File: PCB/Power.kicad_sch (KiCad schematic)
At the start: 27 parts, among them U2 XL4005E1, U3 NCP1117-3.3_SOT223

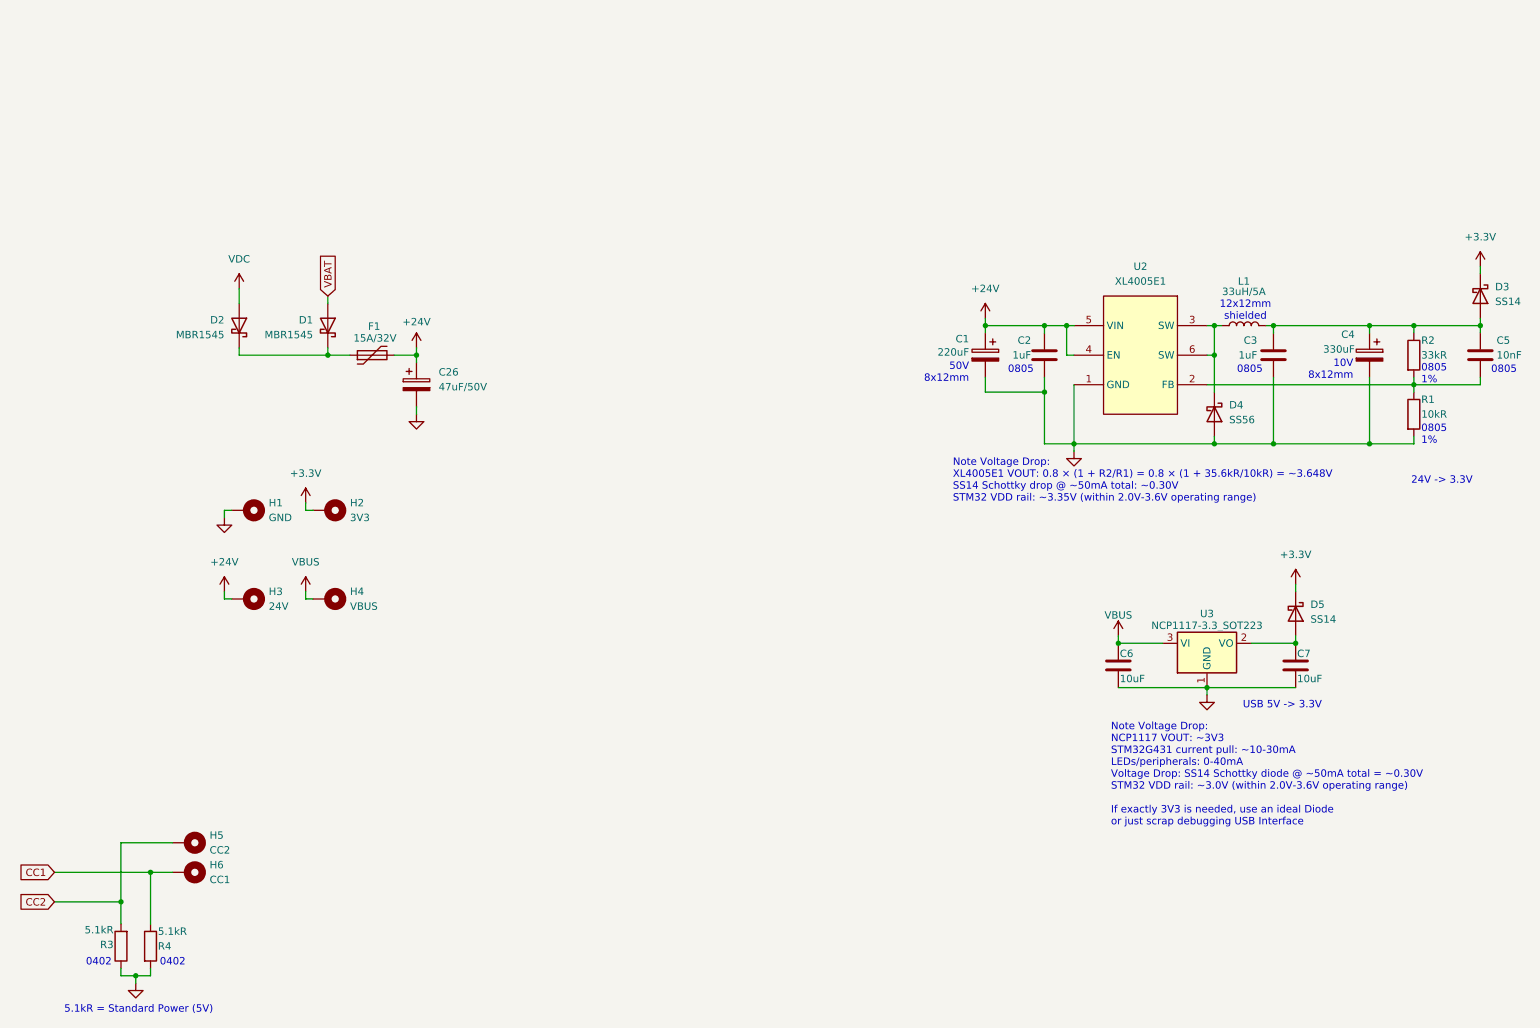
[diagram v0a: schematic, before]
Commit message: Improved Protection and Board Testability - Added power rail protection and decoupling for stepper motor noise environment - Added TVS, bulk caps and fuse upgrade on 24V rail - Added test pads for bring-up and debugging
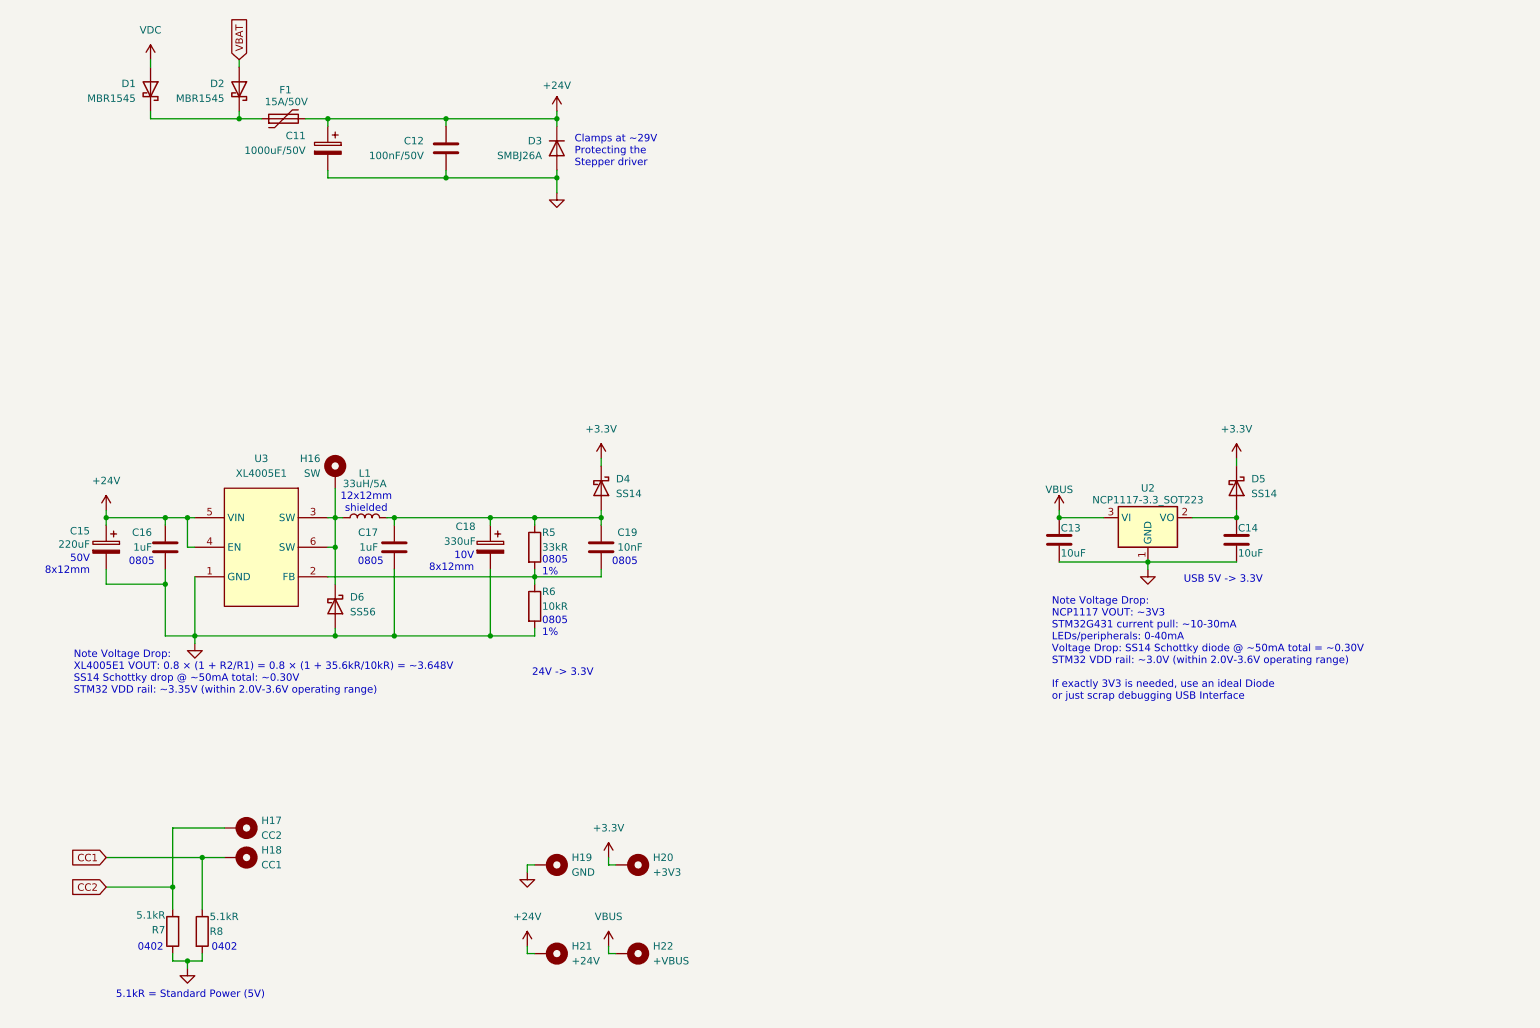
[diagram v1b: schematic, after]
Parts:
- added C12: 100nF/50V, Capacitor_SMD:C_0402_1005Metric, symbol Device:C
- added D3: SMBJ26A, Diode_SMD:D_SMB, symbol Device:D
- added H16: SW, TestPoint:TestPoint_Pad_D1.0mm, symbol Mechanical:MountingHole_Pad
- C11: renamed from C26; value 47uF/50V -> 1000uF/50V; footprint Capacitor_THT:CP_Radial_D8.0mm_P3.50mm -> Capacitor_THT:CP_Radial_D10.0mm_P5.00mm
- F1: value 15A/32V -> 15A/50V
- H17: renamed from H5; footprint TestPoint:TestPoint_Pad_D1.5mm -> TestPoint:TestPoint_Pad_D2.0mm
- H18: renamed from H6; footprint TestPoint:TestPoint_Pad_D1.5mm -> TestPoint:TestPoint_Pad_D2.0mm
- H19: renamed from H1; footprint TestPoint:TestPoint_Pad_D1.5mm -> TestPoint:TestPoint_Pad_D2.0mm
- H20: renamed from H2; value 3V3 -> +3V3; footprint TestPoint:TestPoint_Pad_D1.5mm -> TestPoint:TestPoint_Pad_D2.0mm
- H21: renamed from H3; value 24V -> +24V; footprint TestPoint:TestPoint_Pad_D1.5mm -> TestPoint:TestPoint_Pad_D2.0mm
- H22: renamed from H4; value VBUS -> +VBUS; footprint TestPoint:TestPoint_Pad_D1.5mm -> TestPoint:TestPoint_Pad_D2.0mm
- renumbered C6 to C13, C7 to C14, C1 to C15, C2 to C16, C3 to C17, C4 to C18, C5 to C19, D2 to D1, D1 to D2, D3 to D4, D4 to D6, R2 to R5, R1 to R6, R3 to R7, R4 to R8, U3 to U2, U2 to U3
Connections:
- net +24V: now also C12.1, D3.1 (K)
- net GND: now also C12.2, D3.2 (A)
- net at D6.1 (K), L1.1, U3.3 (SW)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: now also H16.1
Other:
- note added: "Clamps at ~29V Protecting the Stepper driver"
- moved on the sheet: C11, C13, C14, C15, C16, C17, C18, C19, D1, D2, D4, D5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

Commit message: Started laying out the PCB - Decided for a square-shaped board - Split Motor Controllers on top and bottom - Split Power Plane (+3V3 on logic side, +24V on motor side) - Roughly layed out the board entirely - Reconsidered my life choises (got sick)
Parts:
- removed H21: +24V, TestPoint:TestPoint_Pad_D2.0mm, symbol Mechanical:MountingHole_Pad
- added C70: 100nF/50V, Capacitor_SMD:C_0603_1608Metric, symbol Device:C
- added D10: SMBJ26A, Diode_SMD:D_SMB, symbol Device:D
- added H20, H35, H37, H38: +24V, TestPoint:TestPoint_Pad_D2.0mm, symbol Mechanical:MountingHole_Pad
- added H36, H39, H40: GND, TestPoint:TestPoint_Pad_D2.0mm, symbol Mechanical:MountingHole_Pad
- C15: renamed from C12; footprint Capacitor_SMD:C_0402_1005Metric -> Capacitor_SMD:C_0603_1608Metric
- H16: renamed from H17; footprint TestPoint:TestPoint_Pad_D2.0mm -> TestPoint:TestPoint_Pad_D1.0mm
- H17: renamed from H18; footprint TestPoint:TestPoint_Pad_D2.0mm -> TestPoint:TestPoint_Pad_D1.0mm
- renumbered C15 to C11, C16 to C12, C11 to C13, C17 to C14, C18 to C16, C19 to C17, C13 to C18, C14 to C19, D6 to D3, D3 to D4, D4 to D5, D5 to D6, H16 to H18, H20 to H21, R7 to R5, R8 to R6, R5 to R7, R6 to R8, U3 to U2, U2 to U3
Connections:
- net +24V: now also C70.1, D10.1 (K), H20.1, H35.1, H37.1, H38.1
- net GND: now also C70.2, D10.2 (A), H36.1, H39.1, H40.1
- net BIDIR_24V: now reaches D1.1 (K), D2.1 (K), F1.1
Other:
- moved on the sheet: C13, C15, D1, D2, D4, F1, H19, H21, H22

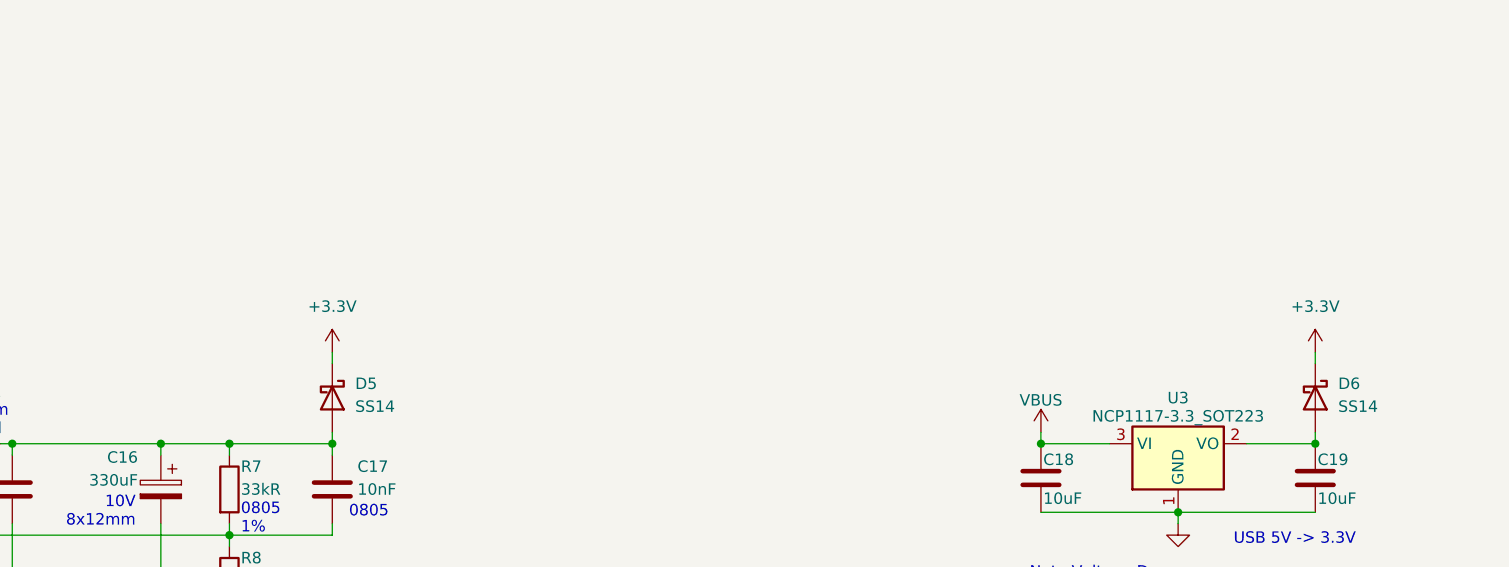
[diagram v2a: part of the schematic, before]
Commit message: Continued PCB Development - Routed MCU decoupeling and Isolated Crystal - Routed LDO Buck converter (VBUS (+5V) -> +3V3) - Routed Buck Converter (+24V -> +3V3) needs review (U2-pin1-GND) - Started Routing TMC2209 to their terminal blocks - Noticed issue with Stepper Lines coupeling back into +24V - TODO: Move Motor Input farther inside and add grounding isolation - Fixed Polariy mismatch with J3 (XT60 Battery Connector)
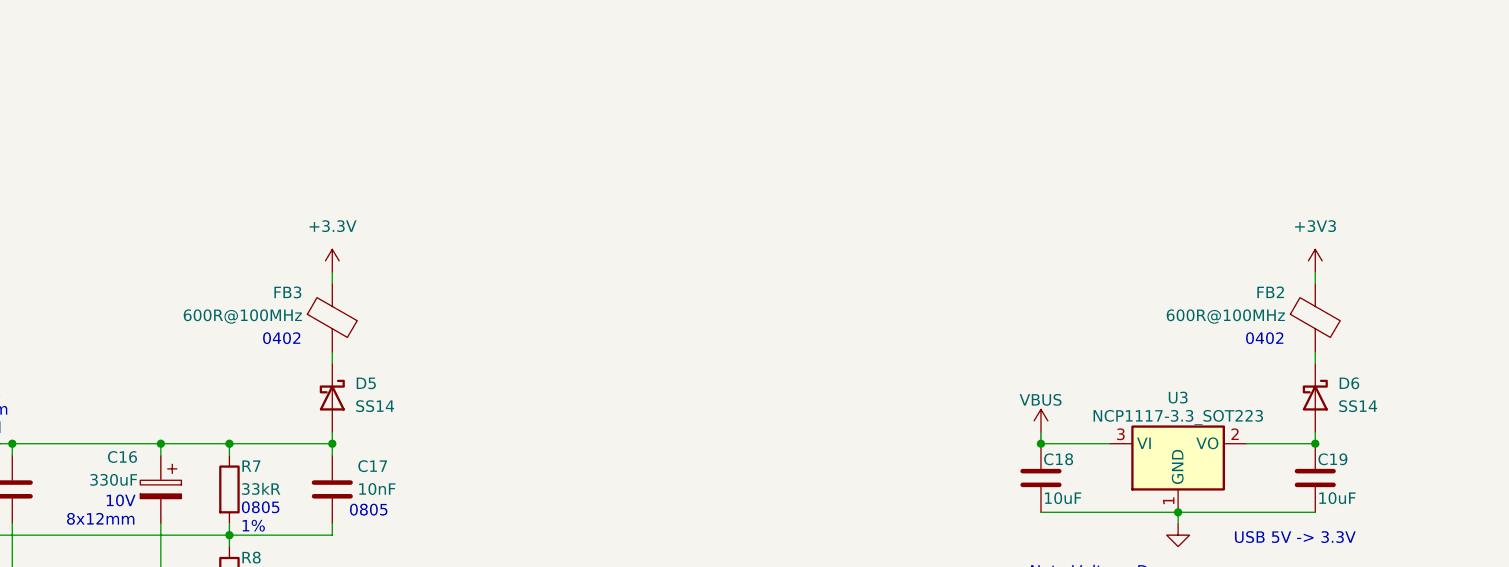
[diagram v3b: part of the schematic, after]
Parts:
- added FB2, FB3: 600R@100MHz, Inductor_SMD:L_0603_1608Metric, symbol Device:FerriteBead
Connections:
- net +3.3V: now also FB3.1; no longer D5.1 (K), D6.1 (K)
- new net: D5.1 (K), FB3.2
- new net: D6.1 (K), FB2.2
- new net +3V3: FB2.1
